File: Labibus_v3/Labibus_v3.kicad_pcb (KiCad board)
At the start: 2 copper layers, 26 parts, among them J1 Screw_Terminal_01x04, SW1 SW_Push, U1 MIC5205-5.0YM5, U2 MAX485E, U3 ATmega328P-AU, Y1 Crystal_GND2_Small

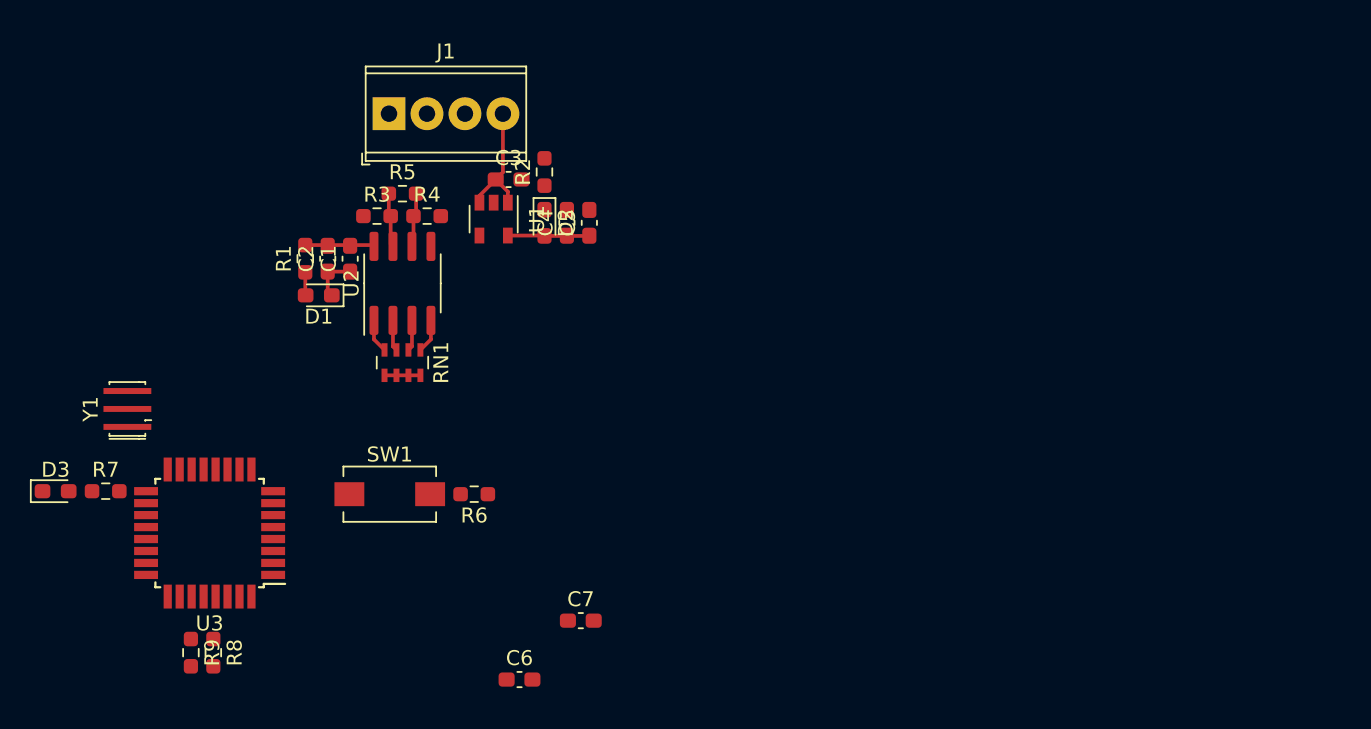
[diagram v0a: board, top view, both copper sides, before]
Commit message: new update to the pcb layout Note: Change pin row to 13 on the left side to shrink the size
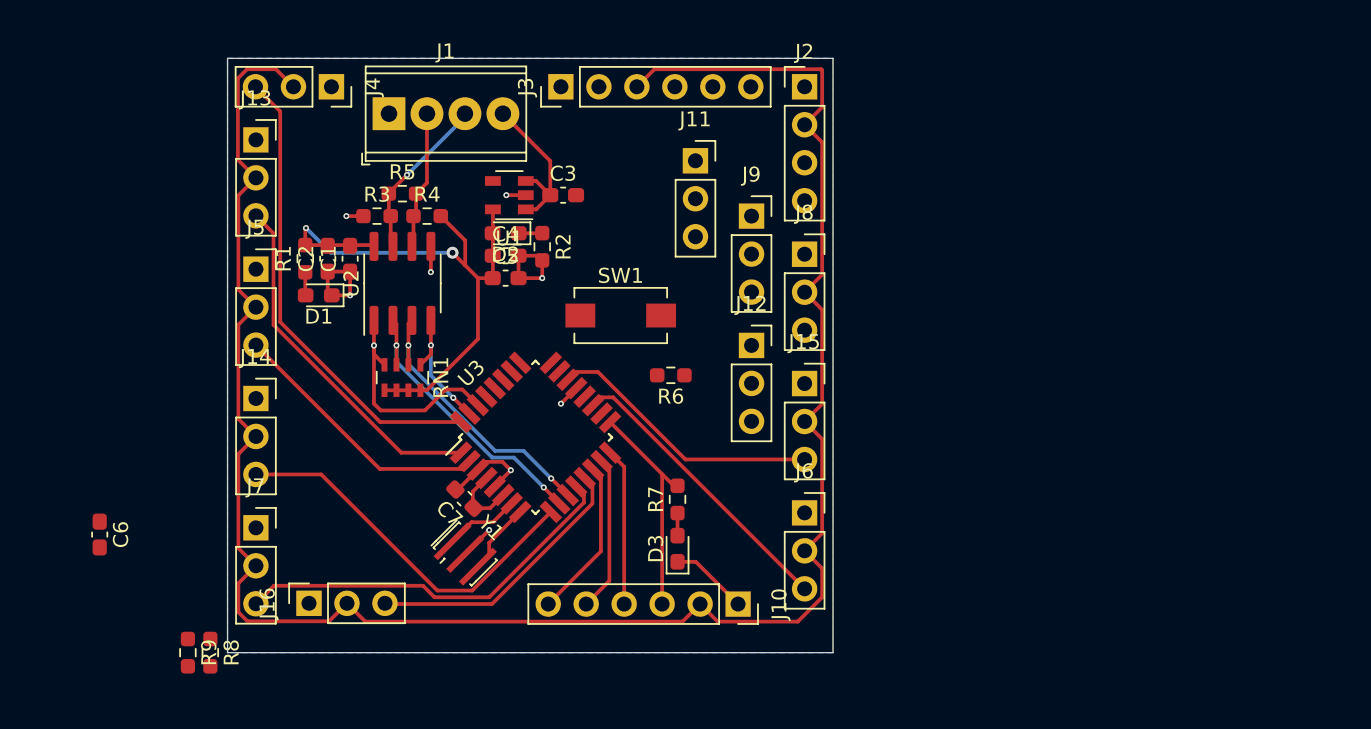
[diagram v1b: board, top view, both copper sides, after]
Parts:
- added J10: Conn_01x06, Connector_PinSocket_2.54mm:PinSocket_1x06_P2.54mm_Vertical, F.Cu at (106.5, 82.4)
- added J11: Conn_01x03, Connector_PinSocket_2.54mm:PinSocket_1x03_P2.54mm_Vertical, F.Cu at (103.6, 52.8)
- added J12: Conn_01x03, Connector_PinSocket_2.54mm:PinSocket_1x03_P2.54mm_Vertical, F.Cu at (107.3, 65.1)
- added J13: Conn_01x03, Connector_PinSocket_2.54mm:PinSocket_1x03_P2.54mm_Vertical, F.Cu at (74.2, 51.4)
- added J14: Conn_01x03, Connector_PinSocket_2.54mm:PinSocket_1x03_P2.54mm_Vertical, F.Cu at (74.2, 68.7)
- added J15: Conn_01x03, Connector_PinSocket_2.54mm:PinSocket_1x03_P2.54mm_Vertical, F.Cu at (110.9, 67.7)
- added J16: Conn_01x03, Connector_PinSocket_2.54mm:PinSocket_1x03_P2.54mm_Vertical, F.Cu at (77.8, 82.3)
- added J2: Conn_01x04, Connector_PinHeader_2.54mm:PinHeader_1x04_P2.54mm_Vertical, F.Cu at (110.9, 47.8)
- added J3: Conn_01x06, Connector_PinHeader_2.54mm:PinHeader_1x06_P2.54mm_Vertical, F.Cu at (94.6, 47.8)
- added J4: Conn_01x03, Connector_PinSocket_2.54mm:PinSocket_1x03_P2.54mm_Vertical, F.Cu at (79.2, 47.8)
- added J5: Conn_01x03, Connector_PinSocket_2.54mm:PinSocket_1x03_P2.54mm_Vertical, F.Cu at (74.2, 60.0)
- added J6: Conn_01x03, Connector_PinSocket_2.54mm:PinSocket_1x03_P2.54mm_Vertical, F.Cu at (110.9, 76.3)
- added J7: Conn_01x03, Connector_PinSocket_2.54mm:PinSocket_1x03_P2.54mm_Vertical, F.Cu at (74.2, 77.3)
- added J8: Conn_01x03, Connector_PinSocket_2.54mm:PinSocket_1x03_P2.54mm_Vertical, F.Cu at (110.9, 59.0)
- added J9: Conn_01x03, Connector_PinSocket_2.54mm:PinSocket_1x03_P2.54mm_Vertical, F.Cu at (107.3, 56.5)
- moved D3 41.8 mm to (102.4, 78.7), turned to 90 degrees
- moved R7 38.3 mm to (102.4, 75.4), turned to 90 degrees
- moved C6 29.7 mm to (63.8, 77.8), turned to 270 degrees
- moved Y1 24.6 mm to (88.2, 79.0), turned to 315 degrees
- moved U3 22.7 mm to (92.9, 71.2), turned to 45 degrees
- moved SW1 19.5 mm to (98.6, 63.1)
- moved R6 15.4 mm to (102.0, 67.1)
- moved C7 11.3 mm to (88.2, 75.3), turned to 135 degrees
- moved C5 6.71 mm to (90.9, 60.6), turned to 0 degrees
- moved R2 5.00 mm to (93.3, 58.5), turned to 270 degrees
- moved C4 4.65 mm to (90.9, 59.1), turned to 0 degrees
- moved C3 3.80 mm to (94.8, 55.0)
- moved D2 2.69 mm to (90.9, 57.6), turned to 180 degrees
- moved U1 1.91 mm to (91.2, 55.0), turned to 180 degrees
- moved RN1 1.00 mm to (84.0, 67.2)
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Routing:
- net +5V: track 12.5 -> 182.9 mm, vias 0 -> 2
- net /D2: track 0.00 -> 31.3 mm
- net GND: track 3.20 -> 31.4 mm, vias 0 -> 8
- net /D8: track 0.00 -> 26.7 mm
- net /D5: track 0.00 -> 25.1 mm
- net /D3: track 0.00 -> 23.9 mm
- net /A6: track 0.00 -> 19.7 mm
- net /D9: track 0.00 -> 18.6 mm
- net /A7: track 0.00 -> 18.5 mm
- net /D4: track 0.00 -> 17.9 mm
- net /ARDUINO_P6: track 2.07 -> 19.0 mm, vias 0 -> 2
- net /ARDUINO_P7: track 2.07 -> 18.6 mm, vias 0 -> 2
- net /SCK: track 0.00 -> 15.0 mm
- net /ARDUINO_P_RX: track 2.27 -> 15.3 mm, vias 0 -> 1
- net /SS: track 0.00 -> 10.7 mm
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- added copper zone on B.Cu, net GND
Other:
- board outline added: 40.5 x 39.8 mm
- rule via_min_drill: 0.3 -> 0.2
- rule via_min_size: 0.4 -> 0.3

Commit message: added tabel and price. board version 1.2
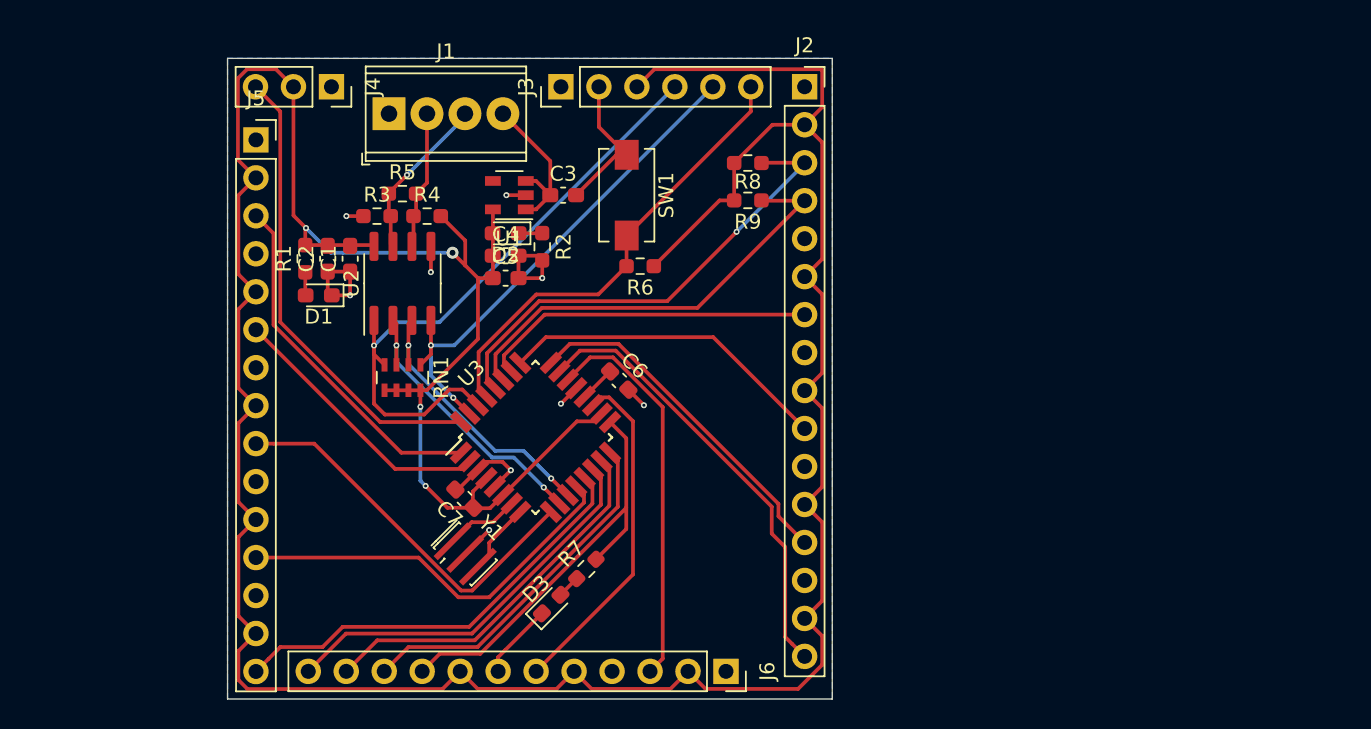
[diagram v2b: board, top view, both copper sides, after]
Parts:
- removed J10: Conn_01x06, Connector_PinSocket_2.54mm:PinSocket_1x06_P2.54mm_Vertical
- removed J11, J12, J13, J14, J15, J16, J7, J8, J9: Conn_01x03, Connector_PinSocket_2.54mm:PinSocket_1x03_P2.54mm_Vertical
- J2: value Conn_01x04 -> Conn_01x16; footprint Connector_PinHeader_2.54mm:PinHeader_1x04_P2.54mm_Vertical -> Connector_PinSocket_2.54mm:PinSocket_1x16_P2.54mm_Vertical
- J5: value Conn_01x03 -> Conn_01x15; footprint Connector_PinSocket_2.54mm:PinSocket_1x03_P2.54mm_Vertical -> Connector_PinSocket_2.54mm:PinSocket_1x15_P2.54mm_Vertical
- J6: value Conn_01x03 -> Conn_01x12; footprint Connector_PinSocket_2.54mm:PinSocket_1x03_P2.54mm_Vertical -> Connector_PinSocket_2.54mm:PinSocket_1x12_P2.54mm_Vertical
- moved R8 48.6 mm to (107.1, 52.9), turned to 180 degrees
- moved R9 48.1 mm to (107.1, 55.4), turned to 180 degrees
- moved C6 36.2 mm to (98.5, 67.5), turned to 315 degrees
- moved J6 11.8 mm to (105.6, 86.9), turned to 270 degrees
- moved D3 9.22 mm to (94.0, 82.4), turned to 45 degrees
- moved J5 8.65 mm to (74.2, 51.4)
- moved SW1 8.06 mm to (99.0, 55.0), turned to 270 degrees
- moved R7 7.67 mm to (96.3, 80.0), turned to 45 degrees
- moved R6 7.58 mm to (99.9, 59.8)
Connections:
- J5 pad 3: /D4 -> /D3
- J6 pad 3: /A6 -> /A7
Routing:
- net +5V: track 182.9 -> 239.3 mm, vias 2 -> 4
- net /A5-SCL: track 0.00 -> 32.0 mm, vias 0 -> 1
- net /DTR: track 0.00 -> 30.9 mm
- net /A0: track 0.00 -> 30.0 mm
- net /A4-SDA: track 0.00 -> 29.8 mm
- net /ARDUINO_P_RX: track 15.3 -> 42.8 mm
- net /ARDUINO_P_TX: track 8.91 -> 34.9 mm
- net /A1: track 0.00 -> 23.5 mm
- net /A3: track 0.00 -> 22.5 mm
- net /A2: track 0.00 -> 22.3 mm
- net /SS: track 10.7 -> 26.8 mm
- net /MOSI: track 10.4 -> 25.4 mm
- net /SCK: track 15.0 -> 28.6 mm
- net /MISO: track 10.5 -> 24.0 mm
- net GND: track 31.4 -> 42.5 mm, vias 8 -> 9
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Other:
- board size 40.5 x 39.8 mm -> 40.5 x 42.9 mm

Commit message: update to PCB, layout update.
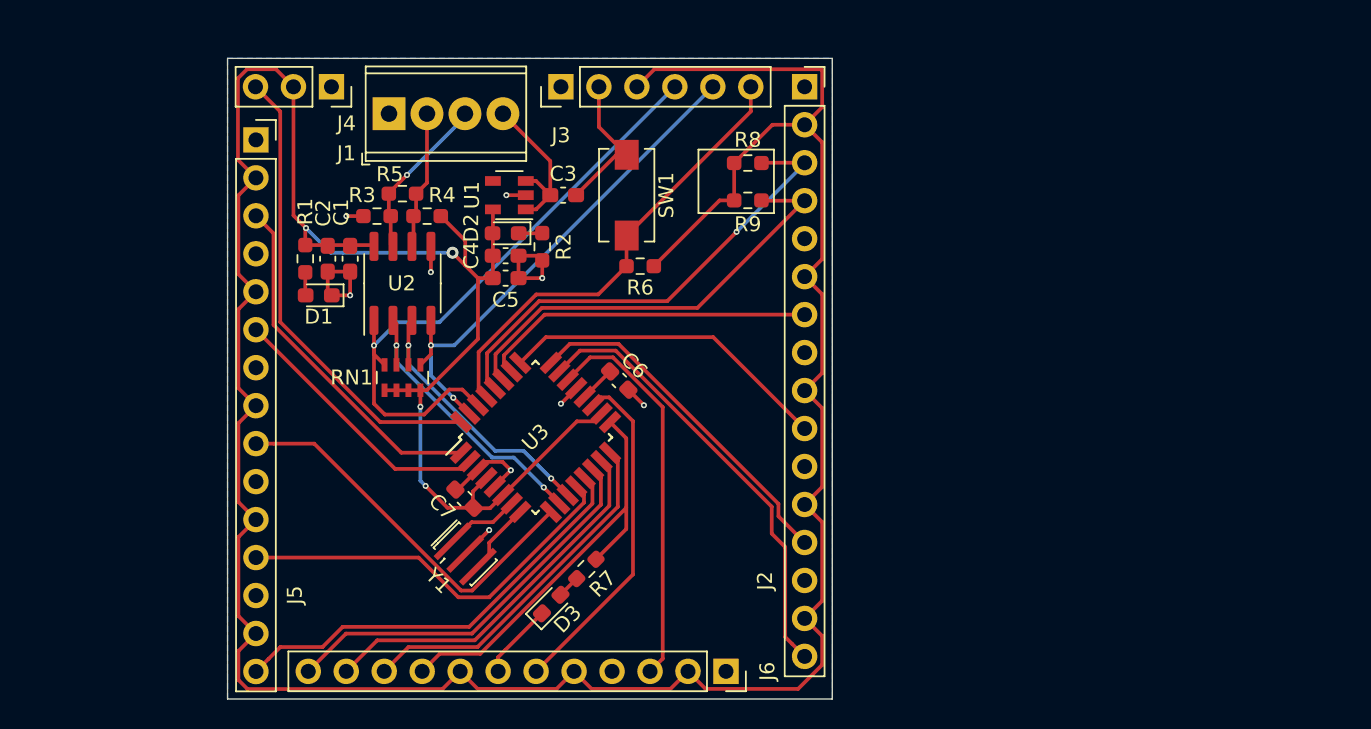
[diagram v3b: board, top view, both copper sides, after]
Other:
- board text added: "5V"
- board text added: "A0"
- board text added: "A1"
- board text added: "A2"
- board text added: "A3"
- board text added: "A6"
- board text added: "A7"
- board text added: "D2"
- board text added: "D3"
- board text added: "D4"
- board text added: "D5"
- board text added: "D8"
- board text added: "D9"
- board text added: "GND"
- board text added: "MISO"
- board text added: "MOSI"
- board text added: "Optional for I2C"
- board text added: "RX"
- board text added: "Reset"
- board text added: "SCK"
- board text added: "SCL"
- board text added: "SDA"
- board text added: "SS"
- board text added: "TX"

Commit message: update to the pcb. 3v3 added I2C 3.3 and 5 JST added.
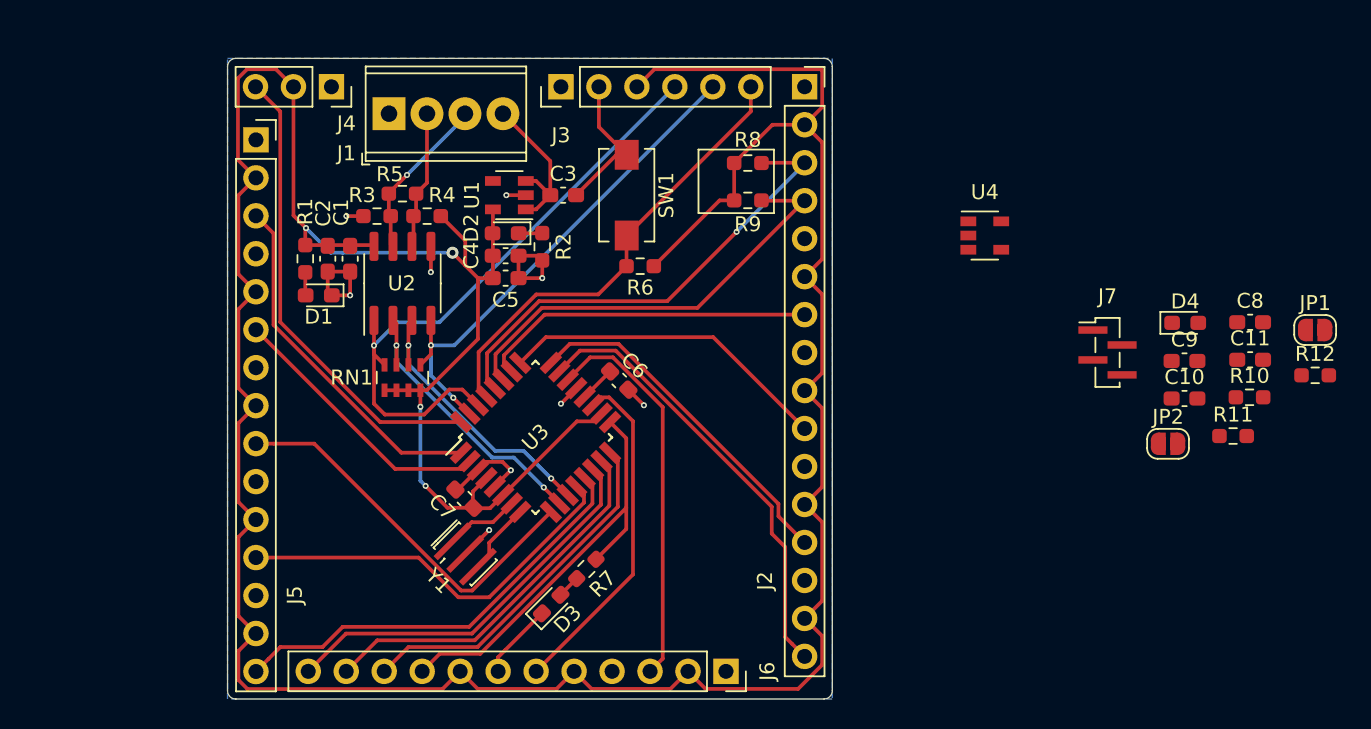
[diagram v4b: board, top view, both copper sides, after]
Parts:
- added C10: 10uF, Capacitor_SMD:C_0603_1608Metric_Pad1.08x0.95mm_HandSolder, F.Cu at (136.3, 68.7)
- added C11: 0.1uF, Capacitor_SMD:C_0603_1608Metric_Pad1.08x0.95mm_HandSolder, F.Cu at (140.7, 66.1)
- added C8: 0.1uF, Capacitor_SMD:C_0603_1608Metric_Pad1.08x0.95mm_HandSolder, F.Cu at (140.7, 63.5)
- added C9: 10uF, Capacitor_SMD:C_0603_1608Metric_Pad1.08x0.95mm_HandSolder, F.Cu at (136.3, 66.1)
- added D4: LED, LED_SMD:LED_0603_1608Metric_Pad1.05x0.95mm_HandSolder, F.Cu at (136.4, 63.6)
- added J7: Conn_01x04 Qwiic JST SH 4-pin, Connector_PinSocket_1.00mm:PinSocket_1x04_P1.00mm_Vertical_SMD_Pin1Left, F.Cu at (131.2, 65.6)
- added JP1: SolderJumper_2_Open, Jumper:SolderJumper-2_P1.3mm_Open_RoundedPad1.0x1.5mm, F.Cu at (145.1, 64.1)
- added JP2: SolderJumper_2_Open, Jumper:SolderJumper-2_P1.3mm_Open_RoundedPad1.0x1.5mm, F.Cu at (135.2, 71.7)
- added R10: 10k, Resistor_SMD:R_0603_1608Metric_Pad0.98x0.95mm_HandSolder, F.Cu at (140.7, 68.6)
- added R11: 10k, Resistor_SMD:R_0603_1608Metric_Pad0.98x0.95mm_HandSolder, F.Cu at (139.6, 71.2)
- added R12: 1k, Resistor_SMD:R_0603_1608Metric_Pad0.98x0.95mm_HandSolder, F.Cu at (145.1, 67.1)
- added U4: MIC5219-3.3YM5, Package_TO_SOT_SMD:SOT-23-5, F.Cu at (123.0, 57.8)
- R2: value 10k -> 1k
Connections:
- J3 pad 2: GND -> Net-(J3-Pad2)
- R6 pad 2: /DTR -> /PC6-RESET
- SW1 pad 2: /DTR -> /PC6-RESET
- U3 pad 29: /DTR -> /PC6-RESET
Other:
- outline, holes or cut-outs redrawn
- board text added: "R5 Optional"

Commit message: testing i can commit, i have commitment issues
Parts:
- moved JP2 30.4 mm to (106.7, 82.3)
- moved U4 26.6 mm to (105.4, 77.7)
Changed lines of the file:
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@@
-(kicad_pcb (version 20171130) (host pcbnew 5.1.10)
+(kicad_pcb (version 20171130) (host pcbnew 5.1.5+dfsg1-2build2)
   (general
     (thickness 1.6)
@@
   )
   (module Package_TO_SOT_SMD:SOT-23-5 (layer F.Cu)
-    (at 122.95 57.75)
+    (at 105.41 77.724)
     (descr "5-pin SOT23 package")
     (tags SOT-23-5)
@@
   )
   (module Jumper:SolderJumper-2_P1.3mm_Open_RoundedPad1.0x1.5mm (layer F.Cu)
-    (at 135.21 71.68)
+    (at 106.68 82.296)
     (descr "SMD Solder Jumper, 1x1.5mm, rounded Pads, 0.3mm gap, open")
     (tags "solder jumper open")

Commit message: new branch test
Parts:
- moved U4 29.1 mm to (120.1, 52.6)
